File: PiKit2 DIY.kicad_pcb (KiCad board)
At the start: 2 copper layers, 56.9 x 66.3 mm, 38 parts, among them J1 Conn_01x06_Socket, J4 USB_C_Receptacle_USB2.0_16P, Q1 2N3904, Q2 2N3904, Q3 2N3906, Q4 2N3904, SW1 SW_Push, U1 PIC18F2550-ISP, X1 20Mhz

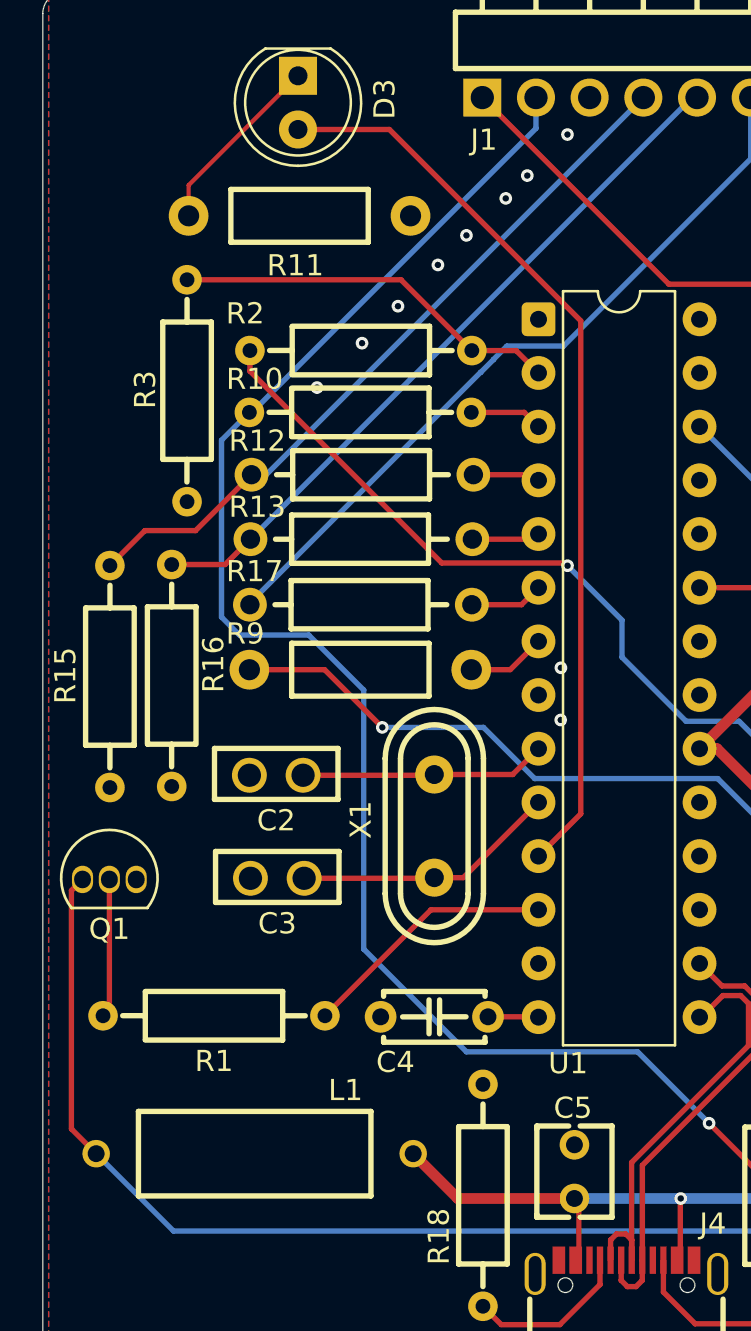
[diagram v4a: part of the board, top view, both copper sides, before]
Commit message: Fixed some DFM violations
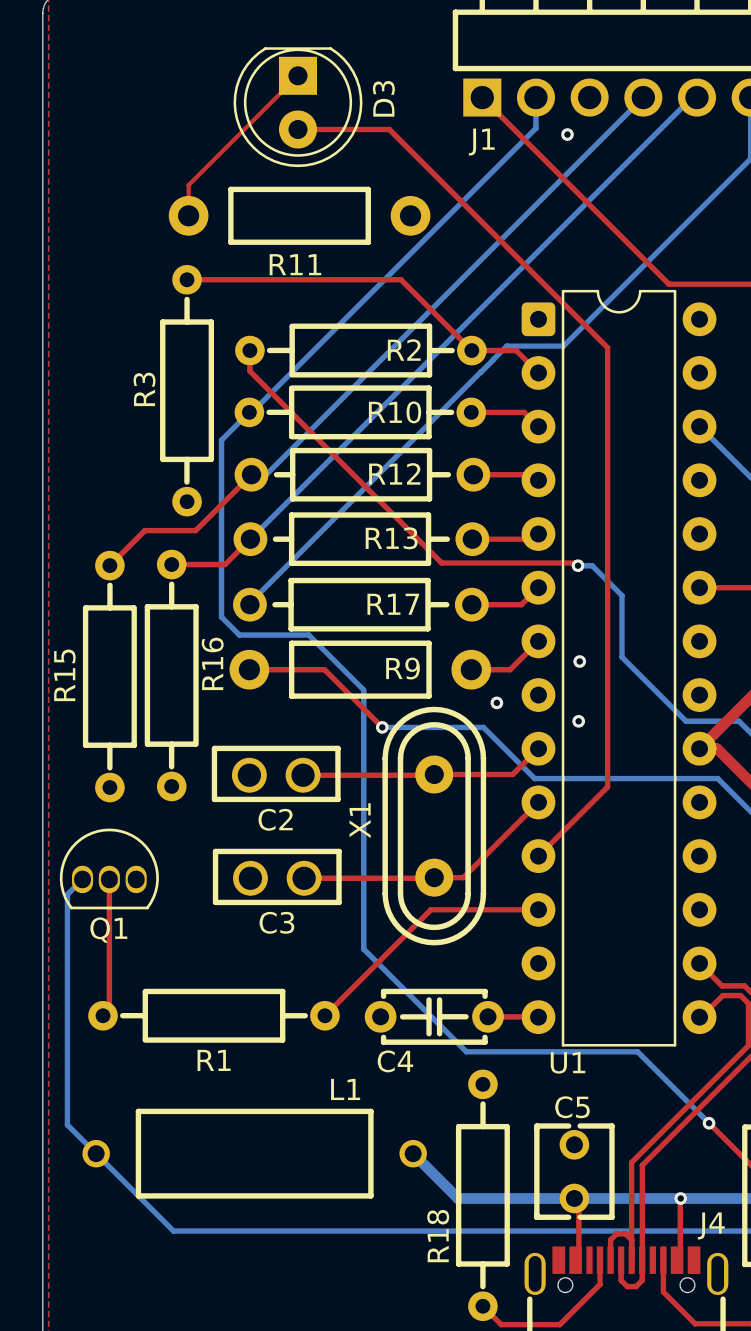
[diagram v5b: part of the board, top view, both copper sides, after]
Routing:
- net 11: track 43.3 -> 44.3 mm
- net Net-(D1-K): track 76.3 -> 77.0 mm
- net GND: vias 10 -> 4
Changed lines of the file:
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@@
 		(tags "C57436 MFR0W4F1002A50 RES-TH_BD2.5-L6.5-P10.50-D0.6 UNI-ROYAL(Uniroyal Elec)")
 		(property "Reference" "R9"
-			(at -5.45 -1.7 0)
+			(at 1.999462 -0.018 0)
 			(layer "F.SilkS")
 			(effects
@@
 		(tags "C119339 CCO(Chian Chia Elec) MF1/4W-4.7KΩ±1% T RES-TH_BD2.3-L6.5-P10.50-D0.5")
 		(property "Reference" "R10"
-			(at 5 1.575 0)
+			(at -1.619462 -0.037 0)
 			(layer "F.SilkS")
 			(effects
@@
 		(tags "C119339 CCO(Chian Chia Elec) MF1/4W-4.7KΩ±1% T RES-TH_BD2.3-L6.5-P10.50-D0.5")
 		(property "Reference" "R2"
-			(at 5.475 1.75 0)
+			(at -2.054462 -0.022 0)
 			(layer "F.SilkS")
 			(effects
@@
 		(tags "C57438 MFR0W4F1000A50 RES-TH_BD2.2-L6.5-P10.50-D0.6 UNI-ROYAL(Uniroyal Elec)")
 		(property "Reference" "R12"
-			(at 4.975 1.6 0)
+			(at -1.529462 -0.007 0)
 			(layer "F.SilkS")
 			(effects
@@
 		(tags "C57438 MFR0W4F1000A50 RES-TH_BD2.2-L6.5-P10.50-D0.6 UNI-ROYAL(Uniroyal Elec)")
 		(property "Reference" "R17"
-			(at 5.025 1.575 0)
+			(at -1.524462 -0.017 0)
 			(layer "F.SilkS")
 			(effects
@@
 		(tags "C57438 MFR0W4F1000A50 RES-TH_BD2.2-L6.5-P10.50-D0.6 UNI-ROYAL(Uniroyal Elec)")
 		(property "Reference" "R13"
-			(at 4.925 1.525 0)
+			(at -1.419462 0.003 0)
 			(layer "F.SilkS")
 			(effects
@@
 	)
 	(segment
-		(start 134.526538 85.921)
-		(end 134.653538 86.048)
-		(width 0.254)
+		(start 156.850538 113.44312)
+		(end 156.850538 113.388)
+		(width 0.381)
 		(layer "F.Cu")
 		(net 1)
 	)
 	(segment
-		(start 119.625538 75.868)
+		(start 128.703538 85.921)
 		(end 119.625538 76.843)
 		(width 0.254)
@@
 	)
 	(segment
-		(start 156.850538 113.44312)
-		(end 156.850538 113.388)
-		(width 0.381)
+		(start 119.625538 76.843)
+		(end 119.625538 75.868)
+		(width 0.254)
 		(layer "F.Cu")
 		(net 1)
@@
 	)
 	(segment
-		(start 128.703538 85.921)
-		(end 134.526538 85.921)
+		(start 162.750658 107.543)
+		(end 156.850538 113.44312)
 		(width 0.254)
 		(layer "F.Cu")
@@
 	)
 	(segment
-		(start 162.750658 107.543)
-		(end 156.850538 113.44312)
+		(start 135.023 85.921)
+		(end 128.703538 85.921)
 		(width 0.254)
 		(layer "F.Cu")
@@
 	)
 	(segment
-		(start 119.625538 76.843)
-		(end 128.703538 85.921)
+		(start 135.15 86.048)
+		(end 135.023 85.921)
 		(width 0.254)
 		(layer "F.Cu")
@@
 	)
 	(via
-		(at 134.653538 86.048)
+		(at 135.15 86.048)
 		(size 0.6)
 		(drill 0.3)
@@
 	)
 	(segment
-		(start 137.230538 90.377233)
-		(end 140.261305 93.408)
+		(start 142.770538 93.408)
+		(end 145.580538 96.218)
 		(width 0.254)
 		(layer "B.Cu")
@@
 	)
 	(segment
-		(start 140.261305 93.408)
-		(end 142.770538 93.408)
+		(start 145.580538 96.218)
+		(end 156.709176 96.218)
 		(width 0.254)
 		(layer "B.Cu")
@@
 	)
 	(segment
-		(start 142.770538 93.408)
-		(end 145.580538 96.218)
+		(start 135.82 86.05)
+		(end 137.230538 87.460538)
 		(width 0.254)
 		(layer "B.Cu")
@@
 	)
 	(segment
-		(start 134.653538 86.048)
-		(end 137.230538 88.625)
+		(start 135.15 86.048)
+		(end 135.152 86.05)
 		(width 0.254)
 		(layer "B.Cu")
@@
 	)
 	(segment
-		(start 145.580538 96.218)
-		(end 156.709176 96.218)
+		(start 137.230538 90.377233)
+		(end 140.261305 93.408)
 		(width 0.254)
 		(layer "B.Cu")
@@
 	)
 	(segment
-		(start 137.230538 88.625)
-		(end 137.230538 90.377233)
+		(start 135.152 86.05)
+		(end 135.82 86.05)
 		(width 0.254)
 		(layer "B.Cu")
 		(net 1)
 	)
-	(via
-		(at 134.650538 65.648)
-		(size 0.6)
-		(drill 0.3)
-		(layers "F.Cu" "B.Cu")
-		(free yes)
-		(net 2)
-	)
-	(via
-		(at 128.520538 71.818)
-		(size 0.6)
-		(drill 0.3)
-		(layers "F.Cu" "B.Cu")
-		(free yes)
-		(net 2)
-	)
-	(via
-		(at 126.630538 73.768)
-		(size 0.6)
-		(drill 0.3)
-		(layers "F.Cu" "B.Cu")
-		(free yes)
-		(net 2)
-	)
-	(via
-		(at 129.870538 70.418)
-		(size 0.6)
-		(drill 0.3)
-		(layers "F.Cu" "B.Cu")
-		(free yes)
-		(net 2)
-	)
-	(via
-		(at 131.730538 68.668)
-		(size 0.6)
-		(drill 0.3)
-		(layers "F.Cu" "B.Cu")
-		(free yes)
-		(net 2)
+	(segment
+		(start 140.261305 93.408)
+		(end 142.770538 93.408)
+		(width 0.254)
+		(layer "B.Cu")
+		(net 1)
 	)
-	(via
-		(at 134.330538 93.348)
-		(size 0.6)
-		(drill 0.3)
-		(layers "F.Cu" "B.Cu")
-		(free yes)
-		(net 2)
+	(segment
+		(start 137.230538 87.460538)
+		(end 137.230538 90.377233)
+		(width 0.254)
+		(layer "B.Cu")
+		(net 1)
 	)
 	(via
-		(at 132.750538 67.588)
+		(at 134.650538 65.648)
 		(size 0.6)
 		(drill 0.3)
@@
 	)
 	(via
-		(at 134.340538 90.878)
+		(at 135.18 93.41)
 		(size 0.6)
 		(drill 0.3)
@@
 	)
 	(via
-		(at 122.800538 77.618)
+		(at 135.23 90.58)
 		(size 0.6)
 		(drill 0.3)
@@
 	)
 	(via
-		(at 124.930538 75.518)
+		(at 131.31 92.54)
 		(size 0.6)
 		(drill 0.3)
@@
 	)
 	(segment
-		(start 129.460538 115.988)
-		(end 134.980538 115.988)
-		(width 0.508)
-		(layer "F.Cu")
-		(net 6)
-	)
-	(segment
 		(start 140.900538 94.708)
 		(end 147.380538 88.228)
@@
 	)
 	(segment
-		(start 127.350538 113.878)
-		(end 129.460538 115.988)
-		(width 0.508)
-		(layer "F.Cu")
-		(net 6)
-	)
-	(segment
 		(start 134.890538 118.908)
 		(end 135.190538 118.908)
@@
 	)
 	(segment
+		(start 134.978538 115.99)
+		(end 134.980538 115.988)
+		(width 0.508)
+		(layer "B.Cu")
+		(net 6)
+	)
+	(segment
 		(start 140.010538 115.988)
 		(end 134.980538 115.988)
@@
 	)
 	(segment
+		(start 127.350538 113.868)
+		(end 129.472538 115.99)
+		(width 0.508)
+		(layer "B.Cu")
+		(net 6)
+	)
+	(segment
 		(start 144.040538 115.988)
 		(end 140.010538 115.988)
@@
 	)
 	(segment
+		(start 129.472538 115.99)
+		(end 134.978538 115.99)
+		(width 0.508)
+		(layer "B.Cu")
+		(net 6)
+	)
+	(segment
 		(start 148.825538 106.268)
 		(end 148.825538 111.203)
@@
 	)
 	(segment
-		(start 111.180538 112.698)
-		(end 112.350538 113.868)
+		(start 161.665538 117.528)
+		(end 116.010538 117.528)
 		(width 0.254)
-		(layer "F.Cu")
+		(layer "B.Cu")
 		(net 7)
 	)
 	(segment
-		(start 111.705538 100.893)
-		(end 111.180538 101.418)
+		(start 163.850538 115.343)
+		(end 161.665538 117.528)
 		(width 0.254)
-		(layer "F.Cu")
+		(layer "B.Cu")
 		(net 7)
 	)
 	(segment
-		(start 111.180538 101.418)
-		(end 111.180538 112.698)
+		(start 116.010538 117.528)
+		(end 112.350538 113.868)
 		(width 0.254)
-		(layer "F.Cu")
+		(layer "B.Cu")
 		(net 7)
 	)
 	(segment
-		(start 161.665538 117.528)
-		(end 116.010538 117.528)
+		(start 110.99 112.507462)
+		(end 112.350538 113.868)
 		(width 0.254)
 		(layer "B.Cu")
@@
 	)
 	(segment
-		(start 163.850538 115.343)
-		(end 161.665538 117.528)
+		(start 111.705538 100.893)
+		(end 110.99 101.608538)
 		(width 0.254)
 		(layer "B.Cu")
@@
 	)
 	(segment
-		(start 116.010538 117.528)
-		(end 112.350538 113.868)
+		(start 110.99 101.608538)
+		(end 110.99 112.507462)
 		(width 0.254)
 		(layer "B.Cu")
@@
 	)
 	(segment
-		(start 135.280538 74.463658)
-		(end 126.22488 65.408)
+		(start 136.55 96.518538)
+		(end 136.55 75.73312)
 		(width 0.254)
 		(layer "F.Cu")
@@
 	)
 	(segment
-		(start 126.22488 65.408)
-		(end 121.900538 65.408)
+		(start 133.280538 99.788)
+		(end 136.55 96.518538)
 		(width 0.254)
 		(layer "F.Cu")
@@
 	)
 	(segment
-		(start 133.280538 99.788)
-		(end 135.280538 97.788)
+		(start 126.22488 65.408)
+		(end 121.900538 65.408)
 		(width 0.254)
 		(layer "F.Cu")
@@
 	)
 	(segment
-		(start 135.280538 97.788)
-		(end 135.280538 74.463658)
+		(start 136.55 75.73312)
+		(end 126.22488 65.408)
 		(width 0.254)
 		(layer "F.Cu")

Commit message: Update PCB layout, DRC rules; remove backup zips
Remove old backup zip archives and apply multiple PCB updates. PiKit2 DIY.kicad_pcb: adjust several component positions (R18, R19, U1...), refresh many element UUIDs, remove/clean up F.SilkS silkscreen lines, and add/modify copper segments/vias and routing to correct nets. Large vertex/path data updated (smoothing/coordinate fixes). PiKit2 DIY.kicad_pro: update DRC exclusions (add hole_clearance entries and several starved_thermal entries for new coordinates) and add a 0.3 entry to the track/pour widths. These changes tidy layout and DRC settings to match the revised routing.
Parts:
- moved R19 1.04 mm to (145.2, 115.7)
- moved R18 0.86 mm to (129.8, 115.7)
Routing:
- net +5V: track 86.5 -> 88.7 mm
- net Net-(J4-CC1): track 7.84 -> 9.05 mm
- net Net-(J4-CC2): track 7.47 -> 8.58 mm
- net GND: track 0.00 -> 0.60 mm
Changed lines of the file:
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@@
 	(footprint "JLCImport:MF1_4W-5_1K_1_T52"
 		(layer "F.Cu")
-		(at 130.650538 115.838 90)
+		(at 129.8 115.71 90)
 		(descr "250mW 5.1kΩ Metal Film Resistor ±1% ±200ppm/℃ 插件,D2.3xL6.5mm Through Hole Resistors ROHS")
 		(tags "C714010 Huaxing Mechanical-Elec. MF1/4W-5.1KΩ±1%T52 RES-TH_BD2.3-L6.5-P10.50-D0.5")
@@
 		)
 		(fp_line
-			(start -6.35 -4.1148)
-			(end -6.35 -10.114813)
-			(stroke
-				(width 0.254)
-				(type solid)
-			)
-			(layer "F.SilkS")
-		)
-		(fp_line
-			(start -3.81 -4.1148)
-			(end -3.81 -10.114813)
-			(stroke
-				(width 0.254)
-				(type solid)
-			)
-			(layer "F.SilkS")
-		)
-		(fp_line
-			(start -1.27 -4.1148)
-			(end -1.27 -10.114813)
-			(stroke
-				(width 0.254)
-				(type solid)
-			)
-			(layer "F.SilkS")
-		)
-		(fp_line
-			(start 1.27 -4.1148)
-			(end 1.27 -10.114813)
-			(stroke
-				(width 0.254)
-				(type solid)
-			)
-			(layer "F.SilkS")
-		)
-		(fp_line
-			(start 3.81 -4.1148)
-			(end 3.81 -10.114813)
-			(stroke
-				(width 0.254)
-				(type solid)
-			)
-			(layer "F.SilkS")
-		)
-		(fp_line
-			(start 6.35 -4.1148)
-			(end 6.35 -10.114813)
-			(stroke
-				(width 0.254)
-				(type solid)
-			)
-			(layer "F.SilkS")
-		)
-		(fp_line
 			(start 7.62 -4.04)
 			(end 7.62 -1.373)
@@
 		(tags "1N5817 C7544876 DO-41_BD2.4-L4.7-P8.70-D0.8-RD LGE")
 		(property "Reference" "D2"
-			(at 0 -2.4 90)
+			(at 0.018 2.414462 90)
 			(layer "F.SilkS")
 			(effects
@@
 		)
 		(fp_line
-			(start -4.572 3.507)
-			(end -4.572 5.08)
-			(stroke
-				(width 0.254)
-				(type solid)
-			)
-			(layer "F.SilkS")
-		)
-		(fp_line
-			(start -4.572 5.08)
-			(end 4.572 5.08)
-			(stroke
-				(width 0.254)
-				(type solid)
-			)
-			(layer "F.SilkS")
-		)
-		(fp_line
 			(start 4.572 1.32334)
 			(end 4.572 -0.573)
@@
 			(layer "F.SilkS")
 		)
-		(fp_line
-			(start 4.572 5.08)
-			(end 4.572 3.507)
-			(stroke
-				(width 0.254)
-				(type solid)
-			)
-			(layer "F.SilkS")
-		)
 		(fp_circle
 			(center -2.89 -1.235)
@@
 	(footprint "JLCImport:MF1_4W-5_1K_1_T52"
 		(layer "F.Cu")
-		(at 144.190538 115.858 90)
+		(at 145.22 115.74 90)
 		(descr "250mW 5.1kΩ Metal Film Resistor ±1% ±200ppm/℃ 插件,D2.3xL6.5mm Through Hole Resistors ROHS")
 		(tags "C714010 Huaxing Mechanical-Elec. MF1/4W-5.1KΩ±1%T52 RES-TH_BD2.3-L6.5-P10.50-D0.5")
@@
 		(tags "THT DIP DIL PDIP 2.54mm 7.62mm 300mil")
 		(property "Reference" "U1"
-			(at 1.4 35.21 0)
+			(at 3.649462 35.552 0)
 			(layer "F.SilkS")
 			(effects
@@
 		(net 1)
 	)
+	(segment
+		(start 140.490538 118.908)
+		(end 140.790538 118.908)
+		(width 0.254)
+		(layer "F.Cu")
+		(net 2)
+	)
+	(segment
+		(start 134.090538 118.908)
+		(end 134.390538 118.908)
+		(width 0.254)
+		(layer "F.Cu")
+		(net 2)
+	)
 	(via
 		(at 134.650538 65.648)
@@
 	)
 	(segment
-		(start 144.190038 97.1675)
-		(end 144.190038 102.905292)
-		(width 0.508)
-		(layer "F.Cu")
-		(net 6)
-	)
-	(segment
 		(start 127.350538 113.868)
 		(end 127.350538 113.878)
@@
 	)
 	(segment
-		(start 140.900538 94.708)
-		(end 141.730538 94.708)
-		(width 0.508)
-		(layer "F.Cu")
-		(net 6)
-	)
-	(segment
 		(start 147.380538 76.298)
 		(end 147.380538 88.228)
@@
 	)
 	(segment
+		(start 148.825538 106.268)
+		(end 147.578 106.268)
+		(width 0.508)
+		(layer "F.Cu")
+		(net 6)
+	)
+	(segment
 		(start 140.900538 94.708)
-		(end 147.380538 88.228)
+		(end 144.190038 91.4185)
 		(width 0.508)
 		(layer "F.Cu")
@@
 	)
 	(segment
-		(start 147.552746 106.268)
-		(end 148.825538 106.268)
+		(start 144.190038 102.880038)
+		(end 144.190038 91.4185)
 		(width 0.508)
 		(layer "F.Cu")
@@
 	)
 	(segment
-		(start 144.190038 102.905292)
-		(end 147.552746 106.268)
+		(start 149.950538 73.708)
+		(end 151.490538 72.168)
 		(width 0.508)
 		(layer "F.Cu")
@@
 	)
 	(segment
-		(start 149.950538 73.708)
-		(end 151.490538 72.168)
-		(width 0.508)
+		(start 134.890538 118.908)
+		(end 135.190538 118.908)
+		(width 0.254)
 		(layer "F.Cu")
 		(net 6)
 	)
 	(segment
-		(start 141.730538 94.708)
-		(end 144.190038 97.1675)
+		(start 147.578 106.268)
+		(end 144.190038 102.880038)
 		(width 0.508)
 		(layer "F.Cu")
@@
 	)
 	(segment
-		(start 134.890538 118.908)
-		(end 135.190538 118.908)
-		(width 0.254)
+		(start 144.190038 91.4185)
+		(end 147.380538 88.228)
+		(width 0.508)
 		(layer "F.Cu")
 		(net 6)
@@
 	)
 	(segment
-		(start 148.825538 111.203)
+		(start 144.040538 115.988)
+		(end 140.010538 115.988)
+		(width 0.508)
+		(layer "B.Cu")
+		(net 6)
+	)
+	(segment
+		(start 149.77 110.258538)
 		(end 144.040538 115.988)
 		(width 0.508)
@@
 	)
 	(segment
-		(start 144.040538 115.988)
-		(end 140.010538 115.988)
+		(start 149.77 107.212462)
+		(end 149.77 110.258538)
 		(width 0.508)
 		(layer "B.Cu")
@@
 	(segment
 		(start 148.825538 106.268)
-		(end 148.825538 111.203)
+		(end 149.77 107.212462)
 		(width 0.508)
 		(layer "B.Cu")
@@
 	)
 	(segment
-		(start 134.290538 121.958)
-		(end 136.190538 120.058)
+		(start 129.8 120.96)
+		(end 130.67 121.83)
 		(width 0.254)
 		(layer "F.Cu")
@@
 	)
 	(segment
-		(start 131.520538 121.958)
-		(end 134.290538 121.958)
+		(start 135.13 121.83)
+		(end 136.190538 120.769462)
 		(width 0.254)
 		(layer "F.Cu")
@@
 	)
 	(segment
-		(start 136.190538 120.058)
+		(start 136.190538 120.769462)
 		(end 136.190538 118.908)
 		(width 0.254)
@@
 	)
 	(segment
-		(start 130.650538 121.088)
-		(end 131.520538 121.958)
+		(start 130.67 121.83)
+		(end 135.13 121.83)
 		(width 0.254)
 		(layer "F.Cu")
@@
 	)
 	(segment
-		(start 140.690538 121.918)
-		(end 139.190598 120.41806)
+		(start 144.48 121.73)
+		(end 145.22 120.99)
 		(width 0.254)
 		(layer "F.Cu")
@@
 	)
 	(segment
-		(start 143.380538 121.918)
-		(end 140.690538 121.918)
+		(start 139.190598 118.908)
+		(end 139.190598 120.740598)
 		(width 0.254)
 		(layer "F.Cu")
@@
 	)
 	(segment
-		(start 144.190538 121.108)
-		(end 143.380538 121.918)
+		(start 139.190598 120.740598)
+		(end 140.18 121.73)
 		(width 0.254)
 		(layer "F.Cu")
@@
 	)
 	(segment
-		(start 139.190598 120.41806)
-		(end 139.190598 118.908)
+		(start 140.18 121.73)
+		(end 144.48 121.73)
 		(width 0.254)
 		(layer "F.Cu")
